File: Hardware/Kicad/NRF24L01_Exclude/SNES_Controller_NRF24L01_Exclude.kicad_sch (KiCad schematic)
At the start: 28 parts, among them J1 Conn_01x07_Socket, J2 Conn_01x08_Socket, Q1 2N7002, Q2 2N7002, Q3 2N7002, SW1 SW_Push, U2 AMS1117-3.3, U3 STM32L412KBTx

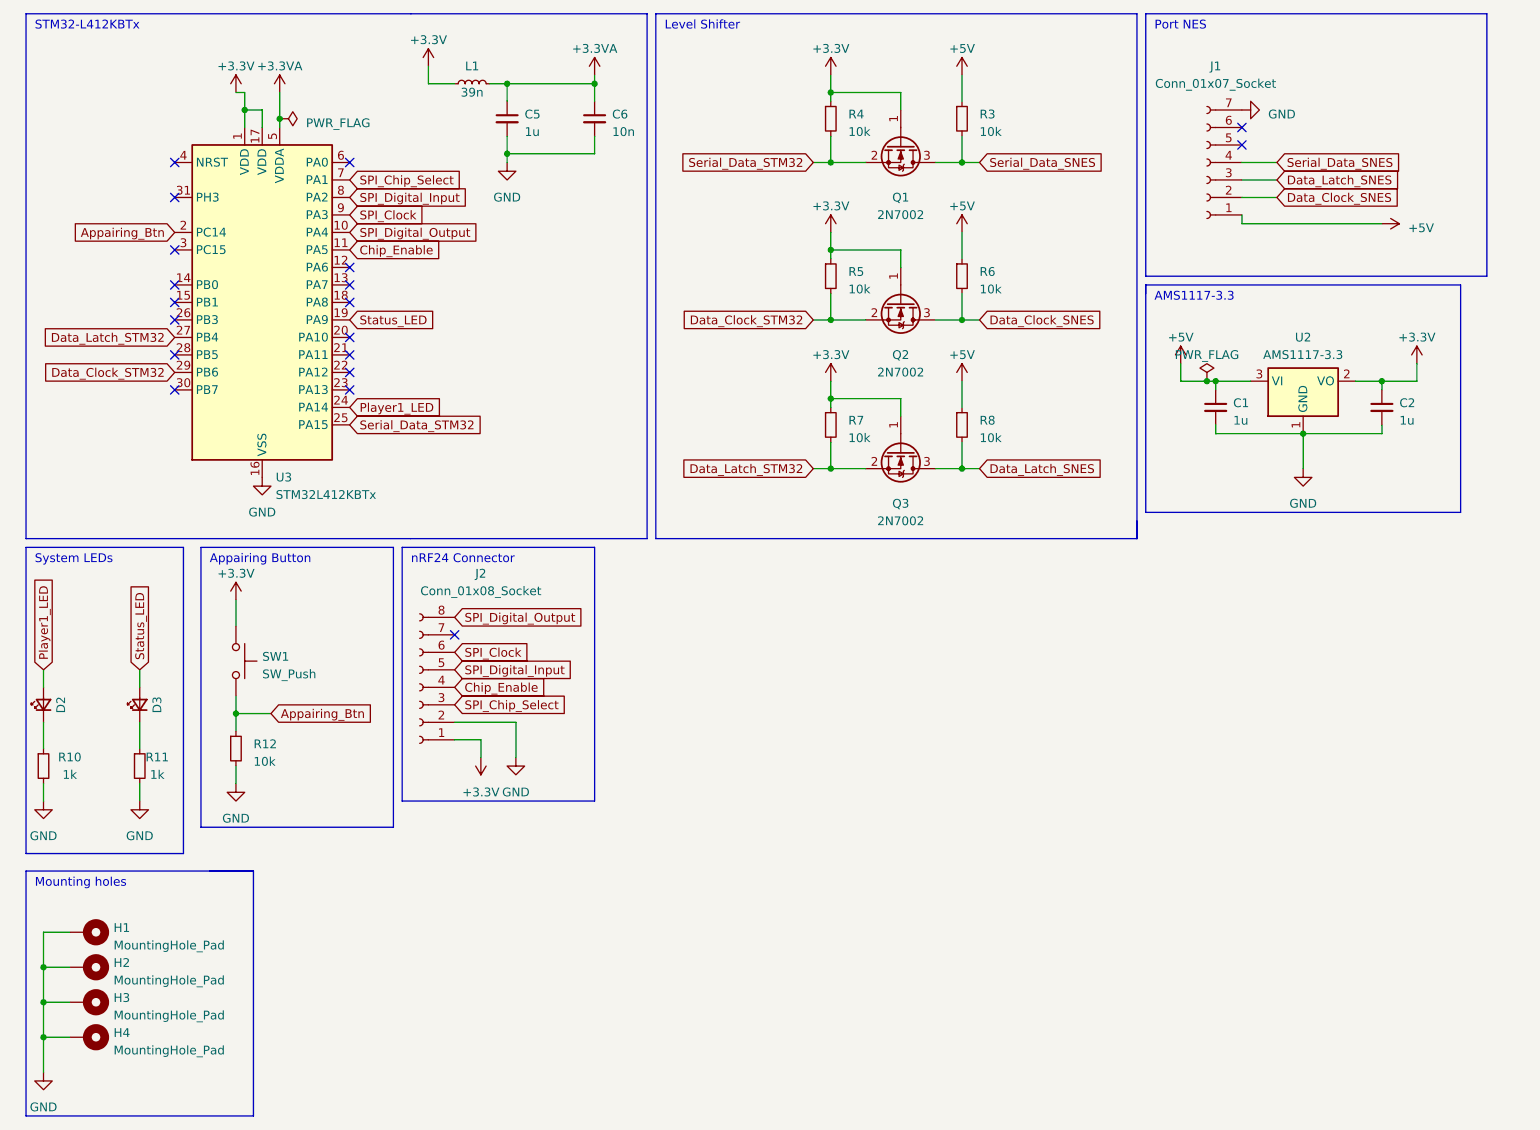
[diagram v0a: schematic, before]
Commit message: Updated NRF24L01 (Exclude & Include) Kicad projects to revision 2.0
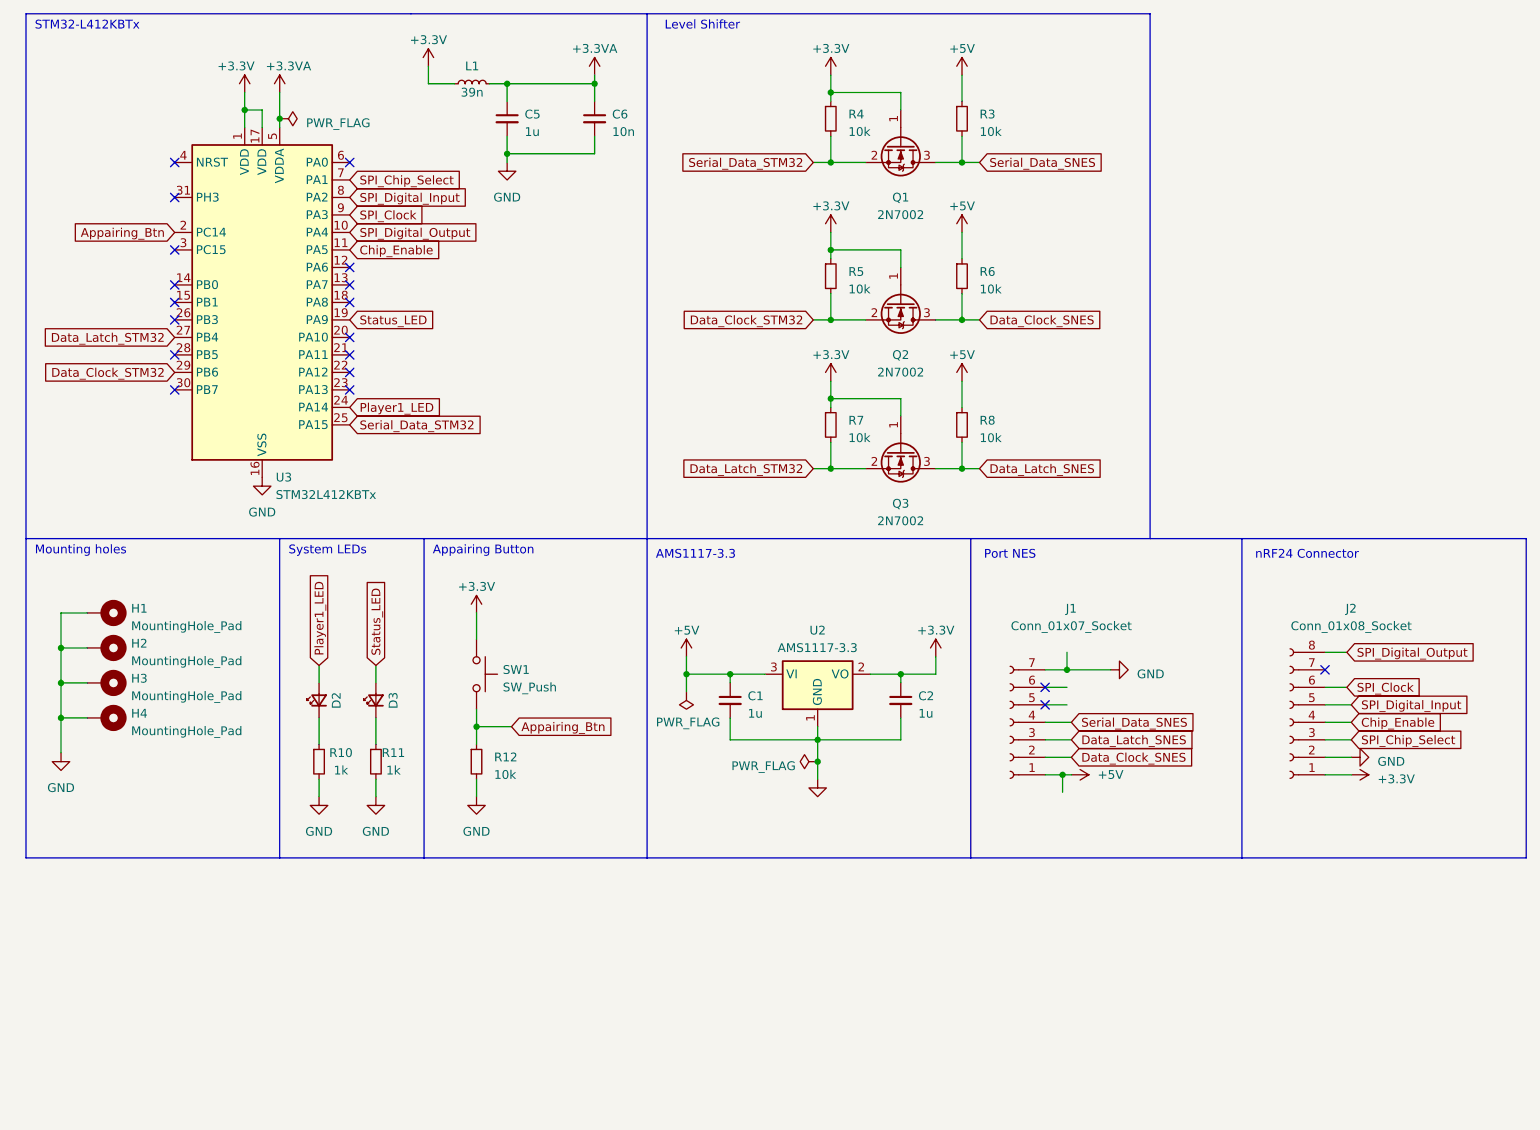
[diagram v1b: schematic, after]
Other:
- company: (none) -> ENSEA
- title: (none) -> SNES Wireless Receiver (NRF24L01 Exclude)
- moved on the sheet: C1, C2, D2, D3, H1, H2, H3, H4, J1, J2, R10, R11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
